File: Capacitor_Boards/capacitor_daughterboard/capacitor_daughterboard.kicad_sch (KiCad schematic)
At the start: 5 parts, among them J1 Conn_01x02_Male, J2 Conn_01x02_Male

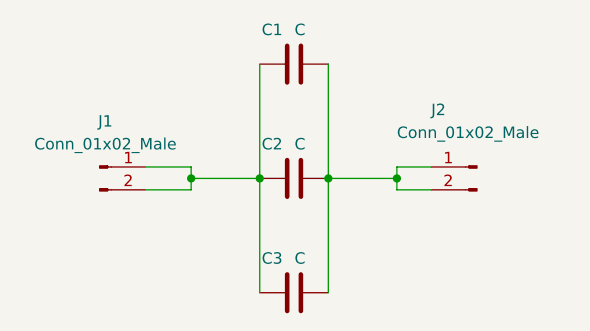
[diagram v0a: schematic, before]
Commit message: resized capacitor daughterboard to have just 2 caps.
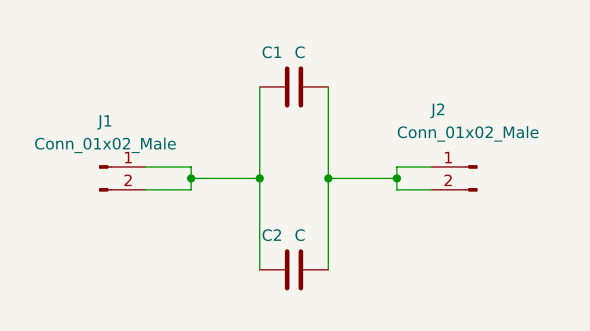
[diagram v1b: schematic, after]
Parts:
- removed C3: C, Capacitor_SMD:C_2225_5664Metric_Pad1.80x6.60mm_HandSolder, symbol Device:C
- C1: footprint (none) -> Capacitor_SMD:C_2225_5664Metric_Pad1.80x6.60mm_HandSolder
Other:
- moved on the sheet: C1, C2
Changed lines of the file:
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@@
+    (stroke (width 0) (type default) (color 0 0 0 0))
+  )
+  (wire (pts (xy 99.06 60.96) (xy 99.06 50.8))
     (stroke (width 0) (type default) (color 0 0 0 0))
   )
@@
     (stroke (width 0) (type default) (color 0 0 0 0))
   )
+  (wire (pts (xy 91.44 60.96) (xy 91.44 50.8))
+    (stroke (width 0) (type default) (color 0 0 0 0))
+  )
   (wire (pts (xy 106.68 49.53) (xy 110.49 49.53))
     (stroke (width 0) (type default) (color 0 0 0 0))
   )
   (wire (pts (xy 78.74 49.53) (xy 83.82 49.53))
-    (stroke (width 0) (type default) (color 0 0 0 0))
-  )
-  (wire (pts (xy 91.44 63.5) (xy 91.44 50.8))
     (stroke (width 0) (type default) (color 0 0 0 0))
   )
@@
     (stroke (width 0) (type default) (color 0 0 0 0))
   )
-  (wire (pts (xy 99.06 38.1) (xy 99.06 50.8))
+  (wire (pts (xy 99.06 40.64) (xy 99.06 50.8))
     (stroke (width 0) (type default) (color 0 0 0 0))
   )
-  (wire (pts (xy 91.44 38.1) (xy 91.44 50.8))
+  (wire (pts (xy 91.44 40.64) (xy 91.44 50.8))
     (stroke (width 0) (type default) (color 0 0 0 0))
   )
@@
     (stroke (width 0) (type default) (color 0 0 0 0))
   )
-  (wire (pts (xy 99.06 50.8) (xy 99.06 63.5))
-    (stroke (width 0) (type default) (color 0 0 0 0))
-  )
   (wire (pts (xy 83.82 50.8) (xy 83.82 52.07))
     (stroke (width 0) (type default) (color 0 0 0 0))
-  )
-  (symbol (lib_id "Device:C") (at 95.25 63.5 90) (unit 1)
-    (in_bom yes) (on_board yes)
-    (property "Reference" "C3" (id 0) (at 93.9799 59.69 90)
-      (effects (font (size 1.27 1.27)) (justify left))
-    )
-    (property "Value" "C" (id 1) (at 96.5199 59.69 90)
-      (effects (font (size 1.27 1.27)) (justify left))
-    )
-    (property "Footprint" "Capacitor_SMD:C_2225_5664Metric_Pad1.80x6.60mm_HandSolder" (id 2) (at 99.06 62.5348 0)
-      (effects (font (size 1.27 1.27)) hide)
-    )
-    (property "Datasheet" "~" (id 3) (at 95.25 63.5 0)
-      (effects (font (size 1.27 1.27)) hide)
-    )
-    (pin "1")
-    (pin "2")
   )
   (symbol (lib_id "Connector:Conn_01x02_Male") (at 115.57 49.53 0) (mirror y) (unit 1)
@@
     (pin "2")
   )
-  (symbol (lib_id "Device:C") (at 95.25 38.1 90) (unit 1)
+  (symbol (lib_id "Device:C") (at 95.25 40.64 90) (unit 1)
     (in_bom yes) (on_board yes)
-    (property "Reference" "C1" (id 0) (at 93.9799 34.29 90)
+    (property "Reference" "C1" (id 0) (at 93.9799 36.83 90)
       (effects (font (size 1.27 1.27)) (justify left))
     )
-    (property "Value" "C" (id 1) (at 96.5199 34.29 90)
+    (property "Value" "C" (id 1) (at 96.5199 36.83 90)
       (effects (font (size 1.27 1.27)) (justify left))
     )
-    (property "Footprint" "" (id 2) (at 99.06 37.1348 0)
+    (property "Footprint" "Capacitor_SMD:C_2225_5664Metric_Pad1.80x6.60mm_HandSolder" (id 2) (at 99.06 39.6748 0)
       (effects (font (size 1.27 1.27)) hide)
     )
-    (property "Datasheet" "~" (id 3) (at 95.25 38.1 0)
+    (property "Datasheet" "~" (id 3) (at 95.25 40.64 0)
       (effects (font (size 1.27 1.27)) hide)
     )
@@
     (pin "2")
   )
-  (symbol (lib_id "Device:C") (at 95.25 50.8 90) (unit 1)
+  (symbol (lib_id "Device:C") (at 95.25 60.96 90) (unit 1)
     (in_bom yes) (on_board yes)
-    (property "Reference" "C2" (id 0) (at 93.9799 46.99 90)
+    (property "Reference" "C2" (id 0) (at 93.9799 57.15 90)
       (effects (font (size 1.27 1.27)) (justify left))
     )
-    (property "Value" "C" (id 1) (at 96.5199 46.99 90)
+    (property "Value" "C" (id 1) (at 96.5199 57.15 90)
       (effects (font (size 1.27 1.27)) (justify left))
     )
-    (property "Footprint" "Capacitor_SMD:C_2225_5664Metric_Pad1.80x6.60mm_HandSolder" (id 2) (at 99.06 49.8348 0)
+    (property "Footprint" "Capacitor_SMD:C_2225_5664Metric_Pad1.80x6.60mm_HandSolder" (id 2) (at 99.06 59.9948 0)
       (effects (font (size 1.27 1.27)) hide)
     )
-    (property "Datasheet" "~" (id 3) (at 95.25 50.8 0)
+    (property "Datasheet" "~" (id 3) (at 95.25 60.96 0)
       (effects (font (size 1.27 1.27)) hide)
     )
@@
       (reference "C2") (unit 1) (value "C") (footprint "Capacitor_SMD:C_2225_5664Metric_Pad1.80x6.60mm_HandSolder")
     )
-    (path "/61b0a90c-0888-4889-b915-b5a54dbc418f"
-      (reference "C3") (unit 1) (value "C") (footprint "Capacitor_SMD:C_2225_5664Metric_Pad1.80x6.60mm_HandSolder")
-    )
     (path "/e96207aa-125f-4a15-ab25-de7b0bdea0cb"

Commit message: Shrunk Daughter Board
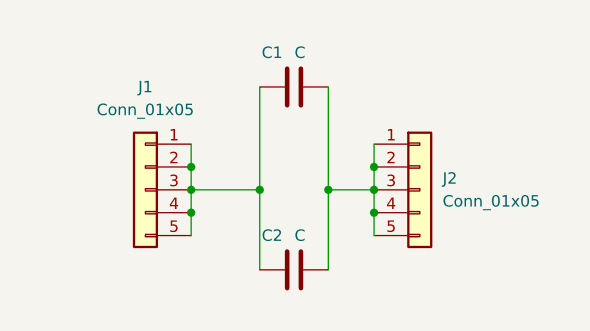
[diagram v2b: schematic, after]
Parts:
- removed J1, J2: Conn_01x02_Male, Connector_PinHeader_2.54mm:PinHeader_1x02_P2.54mm_Vertical, symbol Connector:Conn_01x02_Male
- added J1, J2: Conn_01x05, Connector_PinHeader_2.54mm:PinHeader_1x05_P2.54mm_Vertical, symbol Connector_Generic:Conn_01x05
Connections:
- net at C1.2, C2.2: now also J2.1 (Pin_1), J2.2 (Pin_2), J2.3 (Pin_3), J2.4 (Pin_4), J2.5 (Pin_5)
- net at C1.1, C2.1: now also J1.1 (Pin_1), J1.2 (Pin_2), J1.3 (Pin_3), J1.4 (Pin_4), J1.5 (Pin_5)
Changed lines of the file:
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@@
 (kicad_sch (version 20211123) (generator eeschema)
   (paper "A4")
-  (junction (at 106.68 50.8) (diameter 0) (color 0 0 0 0)
+  (junction (at 104.14 54.61) (diameter 0) (color 0 0 0 0)
   )
-  (junction (at 83.82 50.8) (diameter 0) (color 0 0 0 0)
+  (junction (at 91.44 52.07) (diameter 0) (color 0 0 0 0)
   )
-  (junction (at 91.44 50.8) (diameter 0) (color 0 0 0 0)
+  (junction (at 83.82 52.07) (diameter 0) (color 0 0 0 0)
   )
-  (junction (at 99.06 50.8) (diameter 0) (color 0 0 0 0)
+  (junction (at 83.82 49.53) (diameter 0) (color 0 0 0 0)
   )
-  (wire (pts (xy 83.82 50.8) (xy 91.44 50.8))
+  (junction (at 99.06 52.07) (diameter 0) (color 0 0 0 0)
+  )
+  (junction (at 104.14 49.53) (diameter 0) (color 0 0 0 0)
+  )
+  (junction (at 83.82 54.61) (diameter 0) (color 0 0 0 0)
+  )
+  (junction (at 104.14 52.07) (diameter 0) (color 0 0 0 0)
+  )
+  (wire (pts (xy 83.82 46.99) (xy 83.82 49.53))
     (stroke (width 0) (type default) (color 0 0 0 0))
   )
-  (wire (pts (xy 99.06 60.96) (xy 99.06 50.8))
+  (wire (pts (xy 83.82 52.07) (xy 83.82 54.61))
     (stroke (width 0) (type default) (color 0 0 0 0))
   )
-  (wire (pts (xy 106.68 50.8) (xy 106.68 52.07))
+  (wire (pts (xy 99.06 40.64) (xy 99.06 52.07))
     (stroke (width 0) (type default) (color 0 0 0 0))
   )
-  (wire (pts (xy 83.82 49.53) (xy 83.82 50.8))
+  (wire (pts (xy 83.82 54.61) (xy 83.82 57.15))
     (stroke (width 0) (type default) (color 0 0 0 0))
   )
-  (wire (pts (xy 91.44 60.96) (xy 91.44 50.8))
+  (wire (pts (xy 91.44 40.64) (xy 91.44 52.07))
     (stroke (width 0) (type default) (color 0 0 0 0))
   )
-  (wire (pts (xy 106.68 49.53) (xy 110.49 49.53))
+  (wire (pts (xy 104.14 54.61) (xy 104.14 57.15))
     (stroke (width 0) (type default) (color 0 0 0 0))
   )
-  (wire (pts (xy 78.74 49.53) (xy 83.82 49.53))
+  (wire (pts (xy 91.44 52.07) (xy 91.44 60.96))
     (stroke (width 0) (type default) (color 0 0 0 0))
   )
-  (wire (pts (xy 99.06 50.8) (xy 106.68 50.8))
+  (wire (pts (xy 83.82 49.53) (xy 83.82 52.07))
     (stroke (width 0) (type default) (color 0 0 0 0))
   )
-  (wire (pts (xy 78.74 52.07) (xy 83.82 52.07))
+  (wire (pts (xy 104.14 46.99) (xy 104.14 49.53))
     (stroke (width 0) (type default) (color 0 0 0 0))
   )
-  (wire (pts (xy 99.06 40.64) (xy 99.06 50.8))
+  (wire (pts (xy 99.06 52.07) (xy 99.06 60.96))
     (stroke (width 0) (type default) (color 0 0 0 0))
   )
-  (wire (pts (xy 91.44 40.64) (xy 91.44 50.8))
+  (wire (pts (xy 104.14 49.53) (xy 104.14 52.07))
     (stroke (width 0) (type default) (color 0 0 0 0))
   )
-  (wire (pts (xy 106.68 49.53) (xy 106.68 50.8))
+  (wire (pts (xy 83.82 52.07) (xy 91.44 52.07))
     (stroke (width 0) (type default) (color 0 0 0 0))
   )
-  (wire (pts (xy 106.68 52.07) (xy 110.49 52.07))
+  (wire (pts (xy 104.14 52.07) (xy 104.14 54.61))
     (stroke (width 0) (type default) (color 0 0 0 0))
   )
-  (wire (pts (xy 83.82 50.8) (xy 83.82 52.07))
+  (wire (pts (xy 99.06 52.07) (xy 104.14 52.07))
     (stroke (width 0) (type default) (color 0 0 0 0))
   )
-  (symbol (lib_id "Connector:Conn_01x02_Male") (at 115.57 49.53 0) (mirror y) (unit 1)
-    (in_bom yes) (on_board yes)
-    (property "Reference" "J2" (id 0) (at 110.49 43.18 0)
-      (effects (font (size 1.27 1.27)) (justify right))
+  (symbol (lib_id "Connector_Generic:Conn_01x05") (at 109.22 52.07 0) (unit 1)
+    (in_bom yes) (on_board yes) (fields_autoplaced)
+    (property "Reference" "J2" (id 0) (at 111.76 50.7999 0)
+      (effects (font (size 1.27 1.27)) (justify left))
     )
-    (property "Value" "Conn_01x02_Male" (id 1) (at 106.68 45.72 0)
-      (effects (font (size 1.27 1.27)) (justify right))
+    (property "Value" "Conn_01x05" (id 1) (at 111.76 53.3399 0)
+      (effects (font (size 1.27 1.27)) (justify left))
     )
-    (property "Footprint" "Connector_PinHeader_2.54mm:PinHeader_1x02_P2.54mm_Vertical" (id 2) (at 115.57 49.53 0)
+    (property "Footprint" "Connector_PinHeader_2.54mm:PinHeader_1x05_P2.54mm_Vertical" (id 2) (at 109.22 52.07 0)
       (effects (font (size 1.27 1.27)) hide)
     )
-    (property "Datasheet" "~" (id 3) (at 115.57 49.53 0)
+    (property "Datasheet" "~" (id 3) (at 109.22 52.07 0)
       (effects (font (size 1.27 1.27)) hide)
     )
     (pin "1")
     (pin "2")
+    (pin "3")
+    (pin "4")
+    (pin "5")
   )
-  (symbol (lib_id "Connector:Conn_01x02_Male") (at 73.66 49.53 0) (unit 1)
+  (symbol (lib_id "Connector_Generic:Conn_01x05") (at 78.74 52.07 0) (mirror y) (unit 1)
     (in_bom yes) (on_board yes) (fields_autoplaced)
-    (property "Reference" "J1" (id 0) (at 74.295 44.45 0))
-    (property "Value" "Conn_01x02_Male" (id 1) (at 74.295 46.99 0))
-    (property "Footprint" "Connector_PinHeader_2.54mm:PinHeader_1x02_P2.54mm_Vertical" (id 2) (at 73.66 49.53 0)
+    (property "Reference" "J1" (id 0) (at 78.74 40.64 0))
+    (property "Value" "Conn_01x05" (id 1) (at 78.74 43.18 0))
+    (property "Footprint" "Connector_PinHeader_2.54mm:PinHeader_1x05_P2.54mm_Vertical" (id 2) (at 78.74 52.07 0)
       (effects (font (size 1.27 1.27)) hide)
     )
-    (property "Datasheet" "~" (id 3) (at 73.66 49.53 0)
+    (property "Datasheet" "~" (id 3) (at 78.74 52.07 0)
       (effects (font (size 1.27 1.27)) hide)
     )
     (pin "1")
     (pin "2")
+    (pin "3")
+    (pin "4")
+    (pin "5")
   )
   (symbol (lib_id "Device:C") (at 95.25 40.64 90) (unit 1)
@@
       (reference "C2") (unit 1) (value "C") (footprint "Capacitor_SMD:C_2225_5664Metric_Pad1.80x6.60mm_HandSolder")
     )
-    (path "/e96207aa-125f-4a15-ab25-de7b0bdea0cb"
-      (reference "J1") (unit 1) (value "Conn_01x02_Male") (footprint "Connector_PinHeader_2.54mm:PinHeader_1x02_P2.54mm_Vertical")
+    (path "/ce1a0d46-3821-4556-a718-af5f03e50649"
+      (reference "J1") (unit 1) (value "Conn_01x05") (footprint "Connector_PinHeader_2.54mm:PinHeader_1x05_P2.54mm_Vertical")
     )
-    (path "/8a3edc6b-1900-4f2c-8ac0-275bb3c276eb"
-      (reference "J2") (unit 1) (value "Conn_01x02_Male") (footprint "Connector_PinHeader_2.54mm:PinHeader_1x02_P2.54mm_Vertical")
+    (path "/801f467d-8b5f-4e18-be45-a7b54665a393"
+      (reference "J2") (unit 1) (value "Conn_01x05") (footprint "Connector_PinHeader_2.54mm:PinHeader_1x05_P2.54mm_Vertical")
     )
   )

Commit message: Single pad for caps.
Further reduced size of daughterboard.
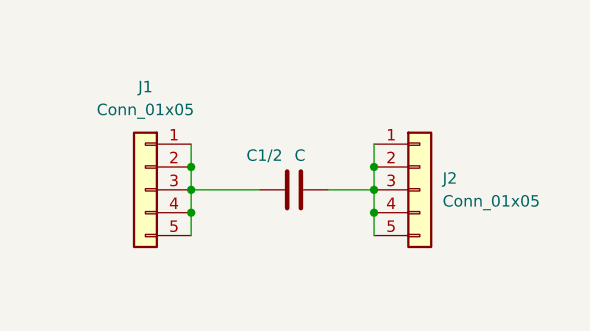
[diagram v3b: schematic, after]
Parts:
- removed C2: C, Capacitor_SMD:C_2225_5664Metric_Pad1.80x6.60mm_HandSolder, symbol Device:C
- renumbered C1 to C1/2
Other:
- moved on the sheet: C1/2
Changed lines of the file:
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@@
   (junction (at 104.14 54.61) (diameter 0) (color 0 0 0 0)
-  )
-  (junction (at 91.44 52.07) (diameter 0) (color 0 0 0 0)
   )
   (junction (at 83.82 52.07) (diameter 0) (color 0 0 0 0)
   )
   (junction (at 83.82 49.53) (diameter 0) (color 0 0 0 0)
-  )
-  (junction (at 99.06 52.07) (diameter 0) (color 0 0 0 0)
   )
   (junction (at 104.14 49.53) (diameter 0) (color 0 0 0 0)
@@
     (stroke (width 0) (type default) (color 0 0 0 0))
   )
-  (wire (pts (xy 99.06 40.64) (xy 99.06 52.07))
-    (stroke (width 0) (type default) (color 0 0 0 0))
-  )
   (wire (pts (xy 83.82 54.61) (xy 83.82 57.15))
     (stroke (width 0) (type default) (color 0 0 0 0))
   )
-  (wire (pts (xy 91.44 40.64) (xy 91.44 52.07))
-    (stroke (width 0) (type default) (color 0 0 0 0))
-  )
   (wire (pts (xy 104.14 54.61) (xy 104.14 57.15))
-    (stroke (width 0) (type default) (color 0 0 0 0))
-  )
-  (wire (pts (xy 91.44 52.07) (xy 91.44 60.96))
     (stroke (width 0) (type default) (color 0 0 0 0))
   )
@@
   )
   (wire (pts (xy 104.14 46.99) (xy 104.14 49.53))
-    (stroke (width 0) (type default) (color 0 0 0 0))
-  )
-  (wire (pts (xy 99.06 52.07) (xy 99.06 60.96))
     (stroke (width 0) (type default) (color 0 0 0 0))
   )
@@
     (pin "5")
   )
-  (symbol (lib_id "Device:C") (at 95.25 40.64 90) (unit 1)
+  (symbol (lib_id "Device:C") (at 95.25 52.07 90) (unit 1)
     (in_bom yes) (on_board yes)
-    (property "Reference" "C1" (id 0) (at 93.9799 36.83 90)
+    (property "Reference" "C1/2" (id 0) (at 93.9799 48.26 90)
       (effects (font (size 1.27 1.27)) (justify left))
     )
-    (property "Value" "C" (id 1) (at 96.5199 36.83 90)
+    (property "Value" "C" (id 1) (at 96.5199 48.26 90)
       (effects (font (size 1.27 1.27)) (justify left))
     )
-    (property "Footprint" "Capacitor_SMD:C_2225_5664Metric_Pad1.80x6.60mm_HandSolder" (id 2) (at 99.06 39.6748 0)
+    (property "Footprint" "Capacitor_SMD:C_2225_5664Metric_Pad1.80x6.60mm_HandSolder" (id 2) (at 99.06 51.1048 0)
       (effects (font (size 1.27 1.27)) hide)
     )
-    (property "Datasheet" "~" (id 3) (at 95.25 40.64 0)
-      (effects (font (size 1.27 1.27)) hide)
-    )
-    (pin "1")
-    (pin "2")
-  )
-  (symbol (lib_id "Device:C") (at 95.25 60.96 90) (unit 1)
-    (in_bom yes) (on_board yes)
-    (property "Reference" "C2" (id 0) (at 93.9799 57.15 90)
-      (effects (font (size 1.27 1.27)) (justify left))
-    )
-    (property "Value" "C" (id 1) (at 96.5199 57.15 90)
-      (effects (font (size 1.27 1.27)) (justify left))
-    )
-    (property "Footprint" "Capacitor_SMD:C_2225_5664Metric_Pad1.80x6.60mm_HandSolder" (id 2) (at 99.06 59.9948 0)
-      (effects (font (size 1.27 1.27)) hide)
-    )
-    (property "Datasheet" "~" (id 3) (at 95.25 60.96 0)
+    (property "Datasheet" "~" (id 3) (at 95.25 52.07 0)
       (effects (font (size 1.27 1.27)) hide)
     )
@@
   (symbol_instances
     (path "/eb0c3764-95bd-4dde-862d-fb130fe53e12"
-      (reference "C1") (unit 1) (value "C") (footprint "Capacitor_SMD:C_2225_5664Metric_Pad1.80x6.60mm_HandSolder")
-    )
-    (path "/fe5f379e-6f71-4bd3-9eb8-4204d8bc6720"
-      (reference "C2") (unit 1) (value "C") (footprint "Capacitor_SMD:C_2225_5664Metric_Pad1.80x6.60mm_HandSolder")
+      (reference "C1/2") (unit 1) (value "C") (footprint "Capacitor_SMD:C_2225_5664Metric_Pad1.80x6.60mm_HandSolder")
     )
     (path "/ce1a0d46-3821-4556-a718-af5f03e50649"
